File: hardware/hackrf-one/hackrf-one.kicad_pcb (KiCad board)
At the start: 4 copper layers, 120 x 75 mm, 432 parts, among them J1 USB-MICRO-B, J10 GND_CLIP, J2 RF-SHIELD-FRAME, J3 RF-SHIELD-COVER, J4 MOUNTING_HOLE, J5 MOUNTING_HOLE, J6 MOUNTING_HOLE, J7 MOUNTING_HOLE, J8 MOUNTING_HOLE, J9 MOUNTING_HOLE, P1 1V8, P13 GPO1, P14 XCVR_CLKOUT, P15 INTR, P16 CLKIN, P17 GPO6, P18 OEB, P19 GPO3, P2 CLKOUT, P20 GPIO, P21 REF_IN, P22 I2S, P23 DBGEN, P24 TRST, P25 LPC_ISP, P26 LPC_JTAG, P27 MIXER_SDATA, P28 SD, P29 CPLD_JTAG, P3 GND, P30 BANK2_AUX, P31 MIXER_SCLK, P32 MIXER_ENX, P33 MIXER_RESETX, P34 MIX_BYPASS, P35 !MIX_BYPASS, P36 VAA, P37 SCL, P38 SDA, P39 SSP1_SCK, P4 ANTENNA, P40 SSP1_MOSI, P41 SSP1_MISO, P42 TX, P43 RX, P44 HP, P45 LP, P46 TX_MIX_BP, P47 RX_MIX_BP, P48 TX_AMP, P49 RX_AMP, P5 LEDS, P50 AMP_BYPASS, P51 !TX_AMP_PWR, P52 !RX_AMP_PWR, P53 CS_XCVR, P54 CS_AD, P55 TXENABLE, P56 RXENABLE, P57 XTAL2, P58 GCK1, P59 GCK2, P6 GPO4, P60 SGPIO_CLK, P61 DA0, P62 DA7, P63 DD0, P64 DD9, P65 DA4, P66 DD5, P67 RSSI, P68 SPIFI_CS, P69 VREGMODE, P7 GPO2, P70 EN_1V8, P71 ID, P72 GP_CLKIN, P73 P1_2, P74 P1_1, P75 GP_CLKIN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

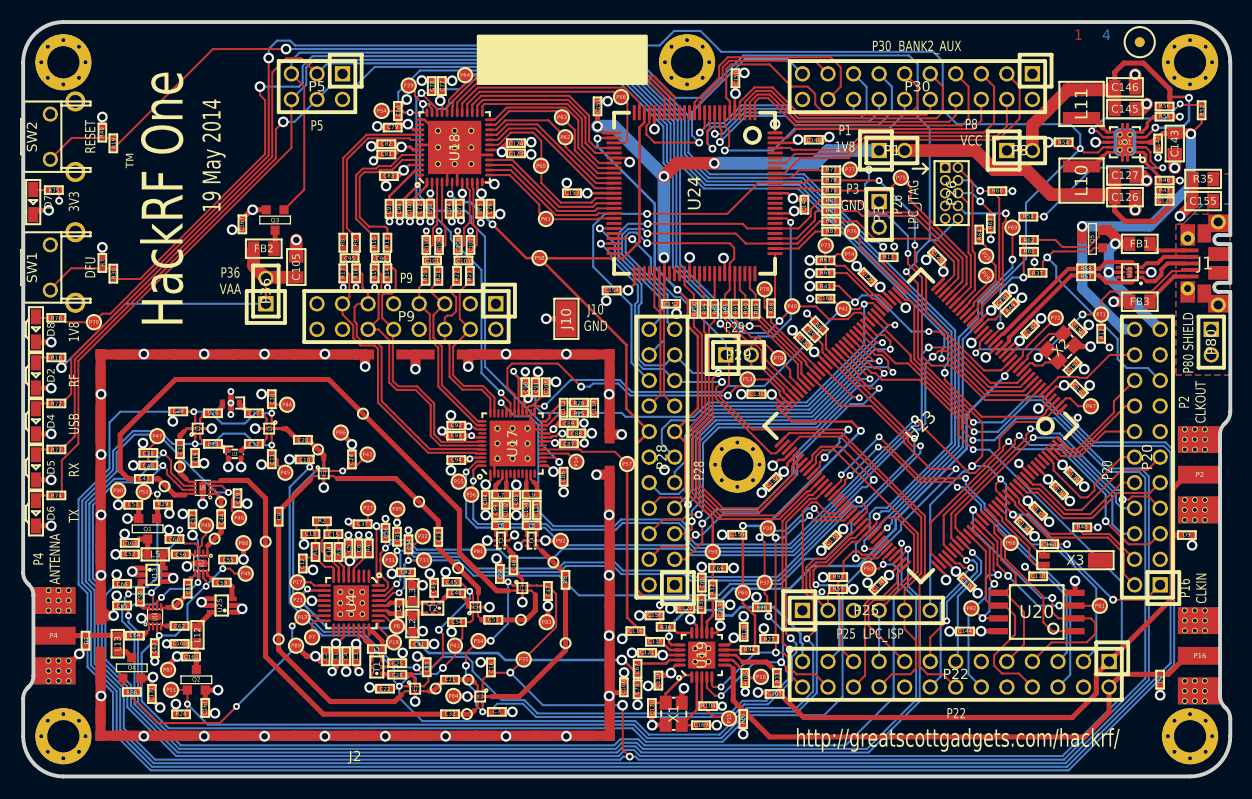
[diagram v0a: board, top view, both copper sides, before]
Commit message: Moved TX Amp and its power switch
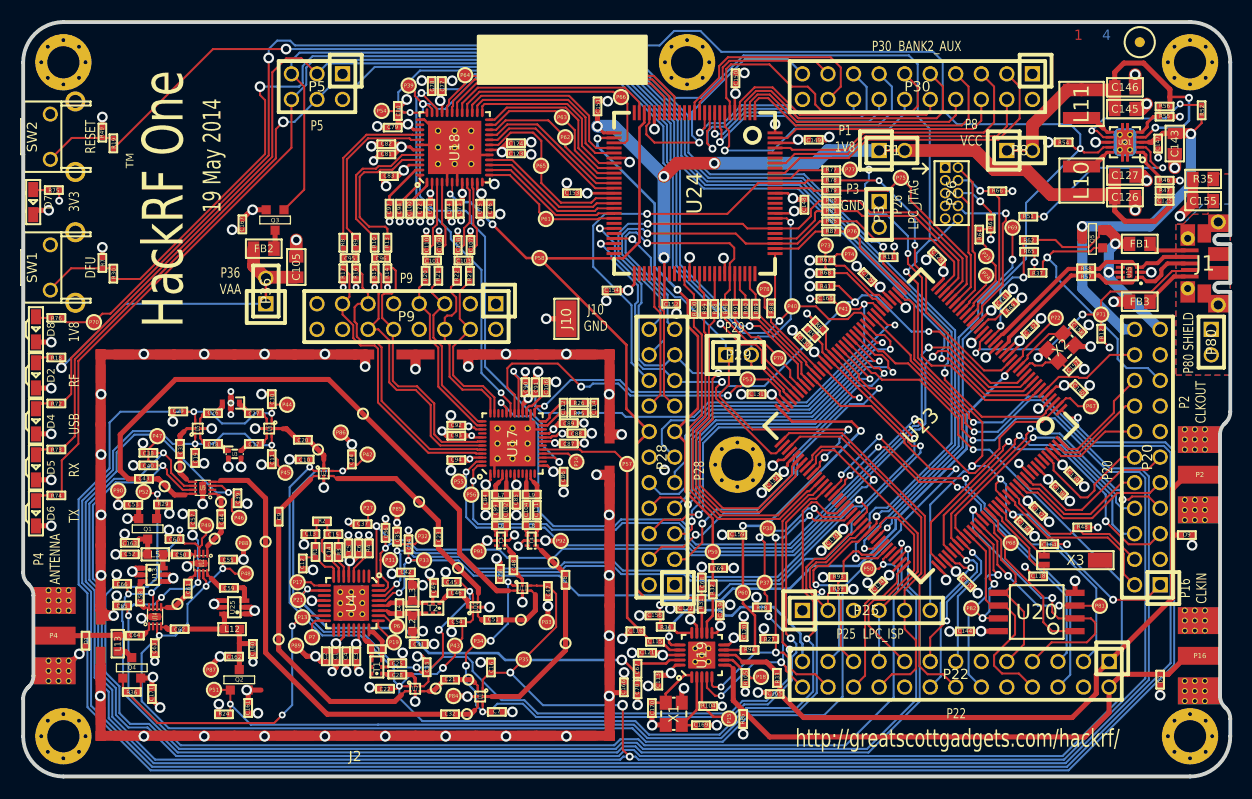
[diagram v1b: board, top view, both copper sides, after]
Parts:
- moved C160 7.31 mm to (82.8, 162.3), turned to 270 degrees
- moved C161 4.27 mm to (82.4, 168.2)
- moved C162 4.27 mm to (81.0, 163.1)
- moved P51 4.27 mm to (79.0, 166.4)
- moved Q2 4.27 mm to (81.5, 165.4)
- moved R24 4.27 mm to (80.0, 168.8)
- moved P87 4.27 mm to (78.7, 164.4)
- moved L12 3.49 mm to (80.8, 160.4), turned to 180 degrees
- moved U25 1.26 mm to (81.0, 158.2)
- moved C59 0.89 mm to (80.5, 156.2)
- moved C62 0.32 mm to (75.6, 160.4)
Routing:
- net !TX_AMP_PWR: track 90.7 -> 86.4 mm
- net /frontend/!ANT_BIAS: track 28.4 -> 31.5 mm
- net Net-(C62-Pad2): track 3.39 -> 5.47 mm
- net Net-(C160-Pad1): track 4.04 -> 5.50 mm
- net RX_MIX_BP: track 192.3 -> 193.4 mm
- net !RX_AMP_PWR: track 130.1 -> 131.2 mm
- net /frontend/TX_AMP_IN: track 1.45 -> 2.38 mm
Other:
- net class Default: clearance 0.1524 -> 0.127
- rule trace_clearance: 0.1524 -> 0.127

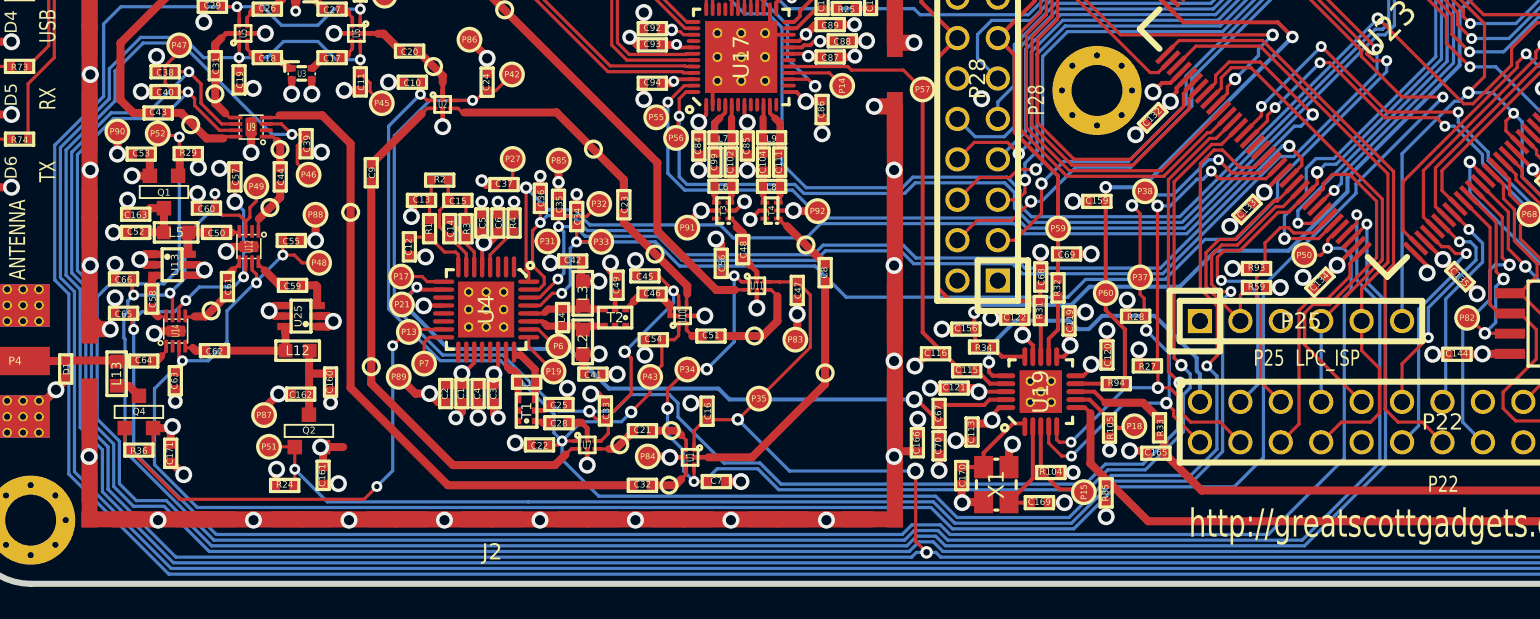
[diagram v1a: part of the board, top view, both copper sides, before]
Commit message: Moved Bias Tee and input switch controls away from signals and Rx amp
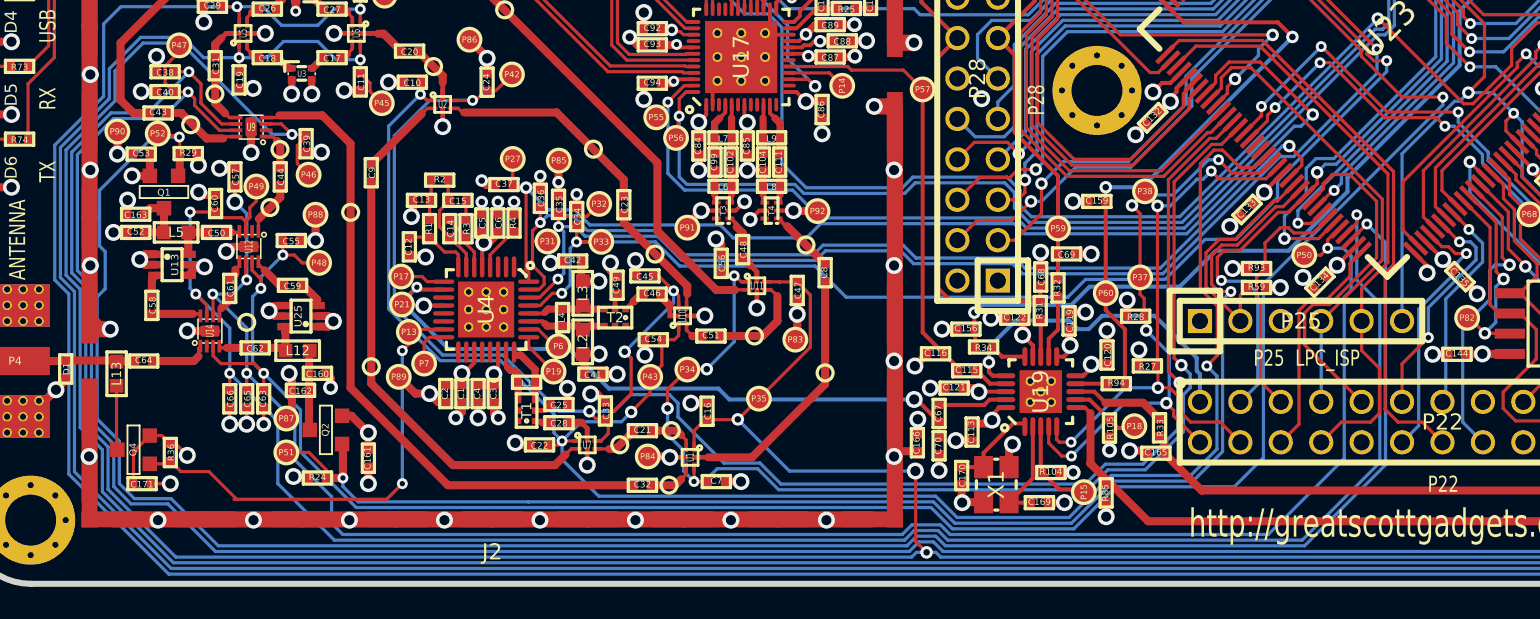
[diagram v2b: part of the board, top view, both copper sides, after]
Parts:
- moved C66 10.1 mm to (76.5, 163.4), turned to 90 degrees
- moved C65 9.42 mm to (77.6, 163.4), turned to 90 degrees
- moved C63 5.67 mm to (78.6, 163.4)
- moved C161 3.04 mm to (85.2, 167.1)
- moved C171 2.63 mm to (71.0, 168.7), turned to 0 degrees
- moved C62 2.56 mm to (78.1, 160.2)
- moved Q4 2.40 mm to (70.5, 166.6), turned to 270 degrees
- moved TESTPOINT-30MIL-MASKONLY 2.35 mm to (77.6, 158.6)
- moved U14 2.15 mm to (75.3, 159.1)
- moved R24 2.11 mm to (82.0, 168.4)
- moved R36 1.98 mm to (72.8, 166.8), turned to 90 degrees
- moved P87 1.41 mm to (80.1, 164.6)
- moved P51 1.15 mm to (80.1, 166.7)
- moved Q2 1.07 mm to (82.6, 165.3), turned to 270 degrees
- moved C160 0.99 mm to (82.0, 161.8), turned to 0 degrees
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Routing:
- net RX_AMP: track 130.3 -> 119.9 mm
- net AMP_BYPASS: track 124.2 -> 114.4 mm
- net TX_AMP: track 143.2 -> 135.0 mm
- net VAA: track 92.7 -> 95.5 mm
- net Net-(L13-Pad1): track 1.66 -> 4.21 mm
- net Net-(C62-Pad2): track 5.47 -> 2.98 mm
- net Net-(C64-Pad1): track 1.52 -> 3.72 mm
- net /frontend/!ANT_BIAS: track 31.5 -> 29.5 mm
- net Net-(C58-Pad1): track 1.24 -> 3.10 mm
- net Net-(C61-Pad1): track 3.22 -> 1.46 mm
- net GND: track 592.3 -> 593.7 mm
- net !RX_AMP_PWR: track 131.2 -> 130.5 mm

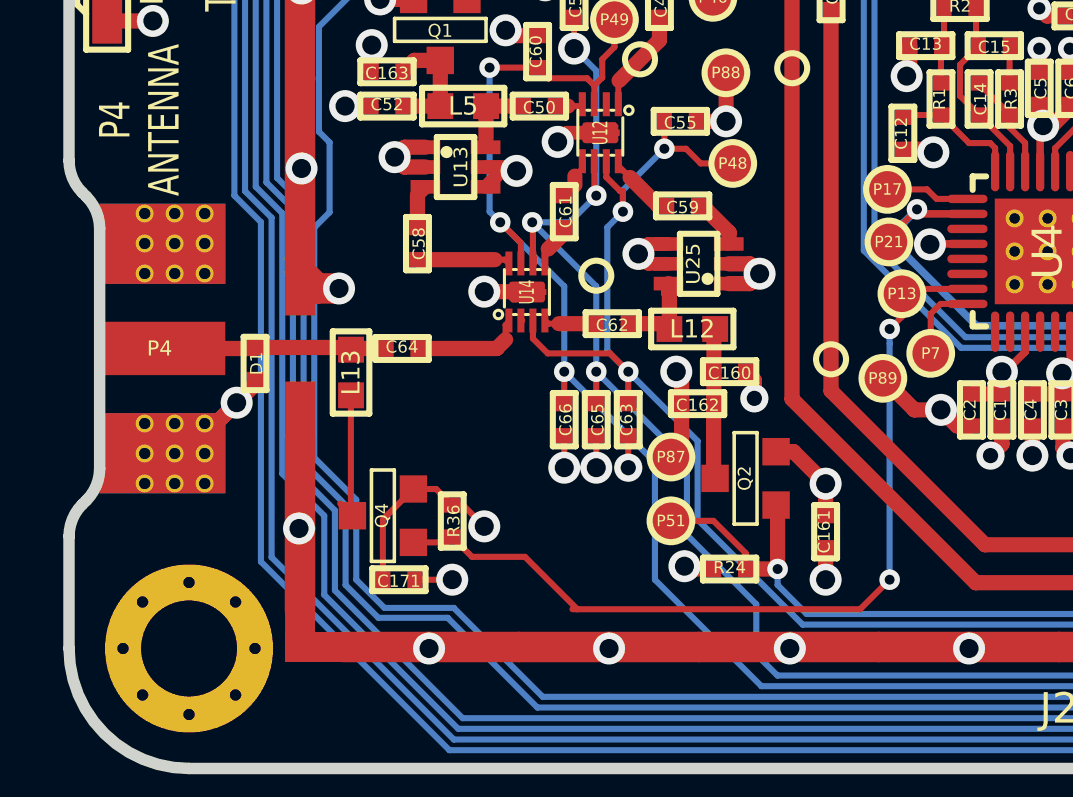
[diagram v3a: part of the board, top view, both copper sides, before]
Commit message: Added protection diodes and related components to schematic. Related (but not the diodes) added to the PCB
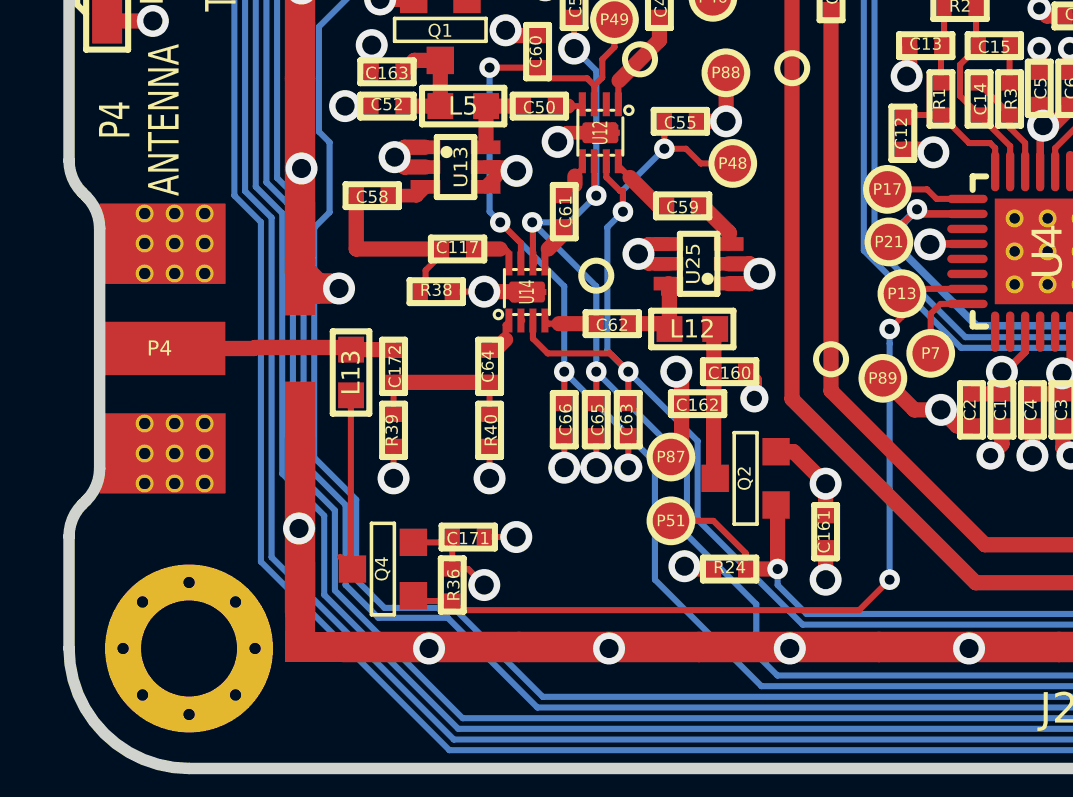
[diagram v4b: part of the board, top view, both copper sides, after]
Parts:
- removed D1: GSG-DIODE-TVS-BI, hackrf:GSG-0402
- added C117: 100nF, hackrf:GSG-0402, F.Cu at (73.0, 157.7)
- added C172: 100nF, hackrf:GSG-0402, F.Cu at (70.8, 161.6)
- added R38: 10k, hackrf:GSG-0402, F.Cu at (72.2, 159.1)
- added R39: 10k, hackrf:GSG-0402, F.Cu at (70.8, 163.7)
- added R40: 10k, hackrf:GSG-0402, F.Cu at (74.0, 163.7)
- C169, C170: value DNP -> 1.8pF
- U15: value LXES1TBCC2-004 -> TVS
- moved C64 2.98 mm to (74.0, 161.6), turned to 270 degrees
- moved C171 2.71 mm to (73.3, 167.3)
- moved C58 2.20 mm to (70.1, 155.9), turned to 0 degrees
- moved R36 2.13 mm to (72.8, 168.9)
- moved Q4 1.78 mm to (70.5, 168.4)
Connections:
- C58 pad 1: Net-(C58-Pad1) -> /frontend/RX_AMP_IN
- C64 pad 2: Net-(C64-Pad2) -> Net-(C172-Pad1)
- L13 pad 2: Net-(C64-Pad2) -> Net-(C172-Pad2)
- P4 pad 1: Net-(C64-Pad2) -> Net-(C172-Pad2)
- U14 pad 8: Net-(C58-Pad1) -> Net-(C117-Pad1)
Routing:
- net Net-(C172-Pad2): track 0.00 -> 7.81 mm
- net Net-(C64-Pad2): track 7.51 -> 0.00 mm
- net /frontend/RX_AMP_IN: track 0.00 -> 6.34 mm
- net Net-(C172-Pad1): track 0.00 -> 5.33 mm
- net GND: track 593.7 -> 589.8 mm
- net Net-(C58-Pad1): track 3.10 -> 0.00 mm
- net Net-(C64-Pad1): track 3.72 -> 1.37 mm
- net Net-(L13-Pad1): track 4.21 -> 5.98 mm
- net VAA: track 95.5 -> 94.0 mm, vias 27 -> 28
- net Net-(C117-Pad1): track 0.00 -> 1.23 mm
- net /frontend/!ANT_BIAS: track 29.5 -> 28.4 mm

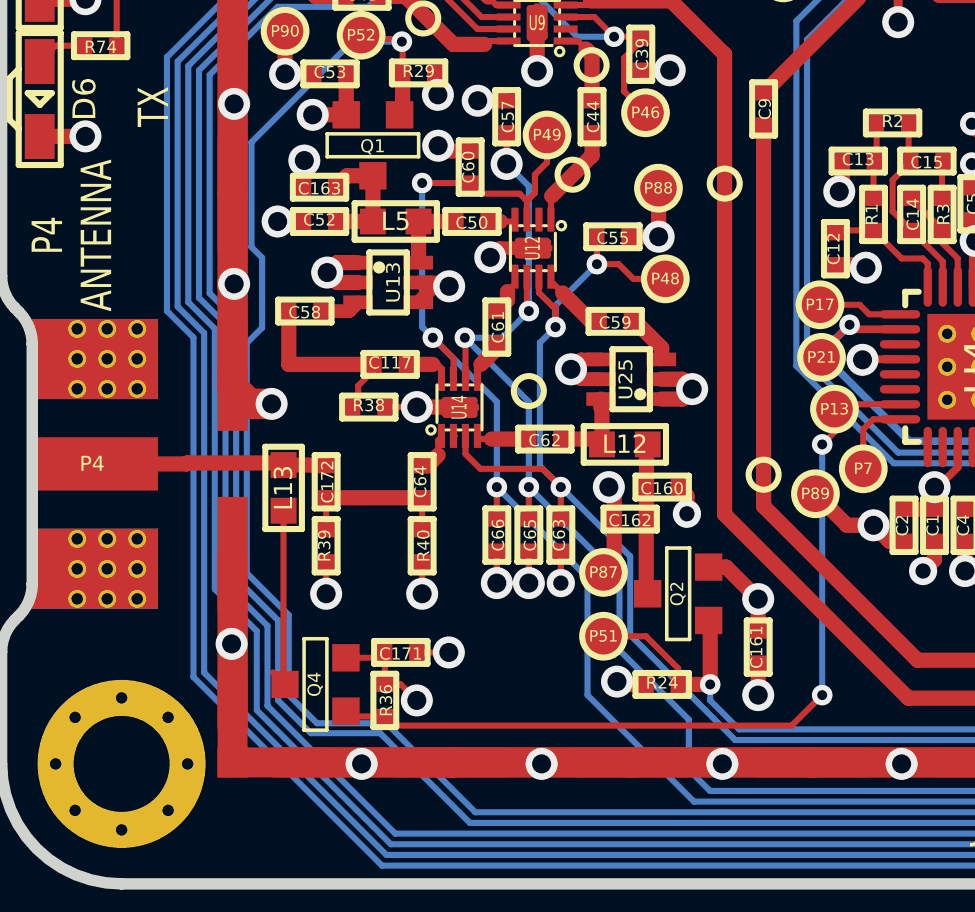
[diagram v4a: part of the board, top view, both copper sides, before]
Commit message: Improved Bias T design to use two inductors
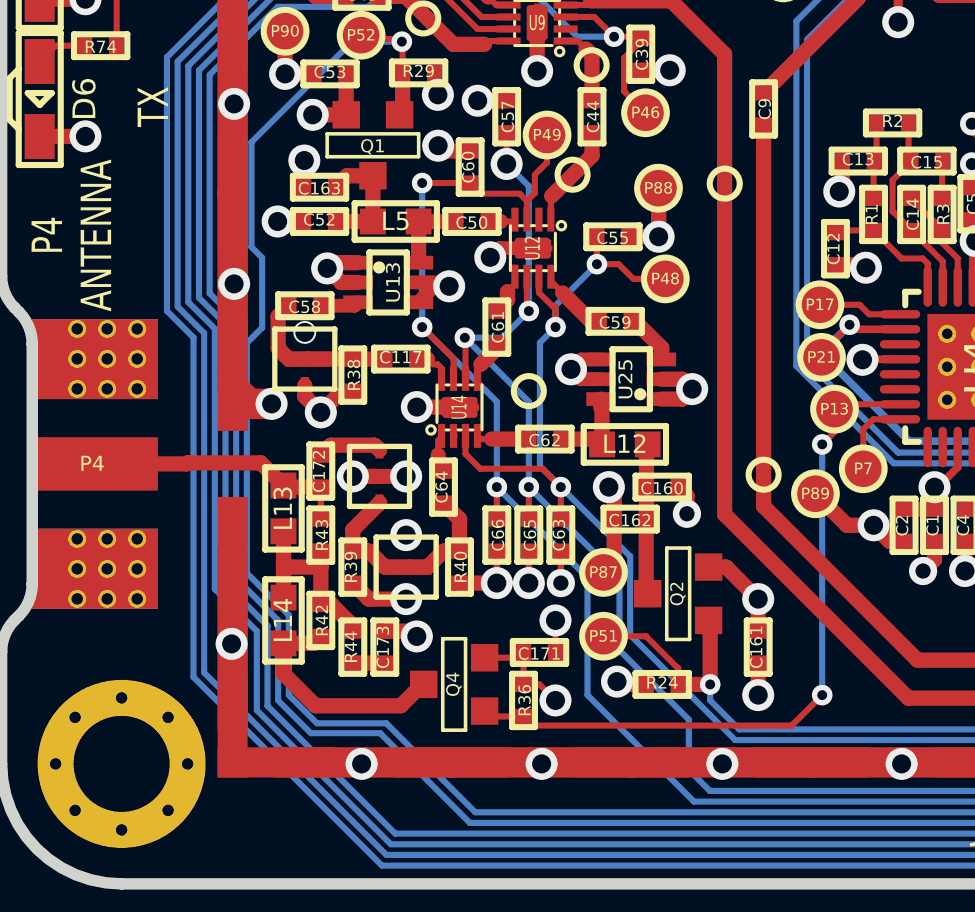
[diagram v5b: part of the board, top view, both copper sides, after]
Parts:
- added C173: 1pF, hackrf:GSG-0402, F.Cu at (72.8, 167.1)
- added D10: SMP1330, gsg-modules:SMP1330-085LF, F.Cu at (70.1, 157.5)
- added D11: SMP1330, gsg-modules:SMP1330-085LF, F.Cu at (73.5, 164.4)
- added D12: SMP1330, gsg-modules:SMP1330-085LF, F.Cu at (72.6, 161.4)
- added L14: 3.3uH, hackrf:GSG-0603, F.Cu at (69.4, 166.2)
- added R42: 1.5k, hackrf:GSG-0402, F.Cu at (70.6, 166.2)
- added R43: 1.5k, hackrf:GSG-0402, F.Cu at (70.6, 163.4)
- added R44: 1.5k, hackrf:GSG-0402, F.Cu at (71.7, 167.1)
- L13: value 10uH -> 0.56uH
- MARK1MM: footprint GSG-MARK1MM -> hackrf:GSG-MARK1MM
- TESTPOINT-30MIL-MASKONLY (x17): footprint GSG-TESTPOINT-30MIL-MASKONLY -> hackrf:GSG-TESTPOINT-30MIL-MASKONLY
- moved C171 4.62 mm to (77.9, 167.3)
- moved Q4 4.62 mm to (75.1, 168.4)
- moved R36 4.62 mm to (77.4, 168.9)
- moved R40 1.43 mm to (75.3, 164.4)
- moved R38 1.19 mm to (71.7, 158.0), turned to 90 degrees
- moved R39 1.14 mm to (71.7, 164.4)
- moved C64 0.73 mm to (74.7, 161.8)
- moved L13 0.68 mm to (69.4, 162.5)
- moved C172 0.40 mm to (70.6, 161.2), turned to 270 degrees
- moved C117 0.40 mm to (73.3, 157.5)
- moved C58 0.18 mm to (70.1, 155.7)
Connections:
- Q4 pad D: Net-(L13-Pad1) -> Net-(L14-Pad1)
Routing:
- net Net-(L14-Pad1): track 0.00 -> 7.77 mm
- net Net-(C172-Pad1): track 5.33 -> 9.96 mm
- net /frontend/!ANT_BIAS: track 28.4 -> 23.8 mm
- net GND: track 589.8 -> 593.3 mm, vias 230 -> 234
- net Net-(C172-Pad2): track 7.81 -> 8.94 mm
- net VAA: track 94.0 -> 95.1 mm, vias 28 -> 29
- net /frontend/RX_AMP_IN: track 6.34 -> 5.27 mm
- net Net-(C173-Pad2): track 0.00 -> 1.07 mm
- net Net-(L13-Pad1): track 5.98 -> 6.85 mm
- net Net-(C117-Pad1): track 1.23 -> 0.70 mm
- net RX_AMP: track 119.9 -> 120.4 mm
